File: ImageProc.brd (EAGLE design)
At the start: 44 x 23.2 mm, 96 parts, among them IC1 XC61GC3002HR-G, IC2 MIC5335-SPYMT, IC3 LTC6087, IC4 LTC6087, IC5 AT86RF233-ZU, IC7 DRV8833RTY, IC8 DRV8833RTY, IC9 MPU-6000, J1 CON-HRS-DM3AT, P1 BAT+, P10 MD2, P2 BAT-, P3 MA1, P4 MA2, P5 MB1, P6 MB2, P7 MC1, P8 MC2, P9 MD1, U1 CY8C5688LTI-LP086, U2 SIT8008AI-72-33E-24.000000G

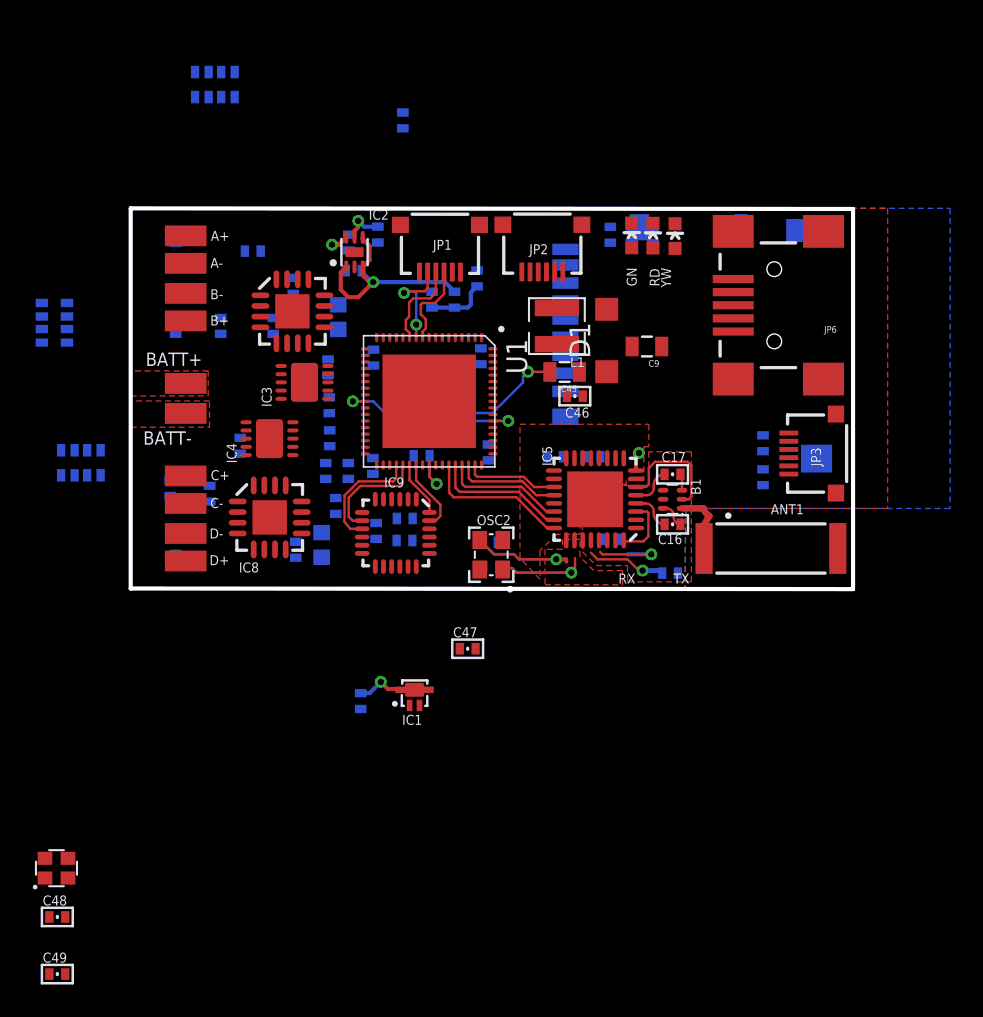
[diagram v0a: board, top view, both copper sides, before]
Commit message: Further routing. Moved 1K resistors to res array.
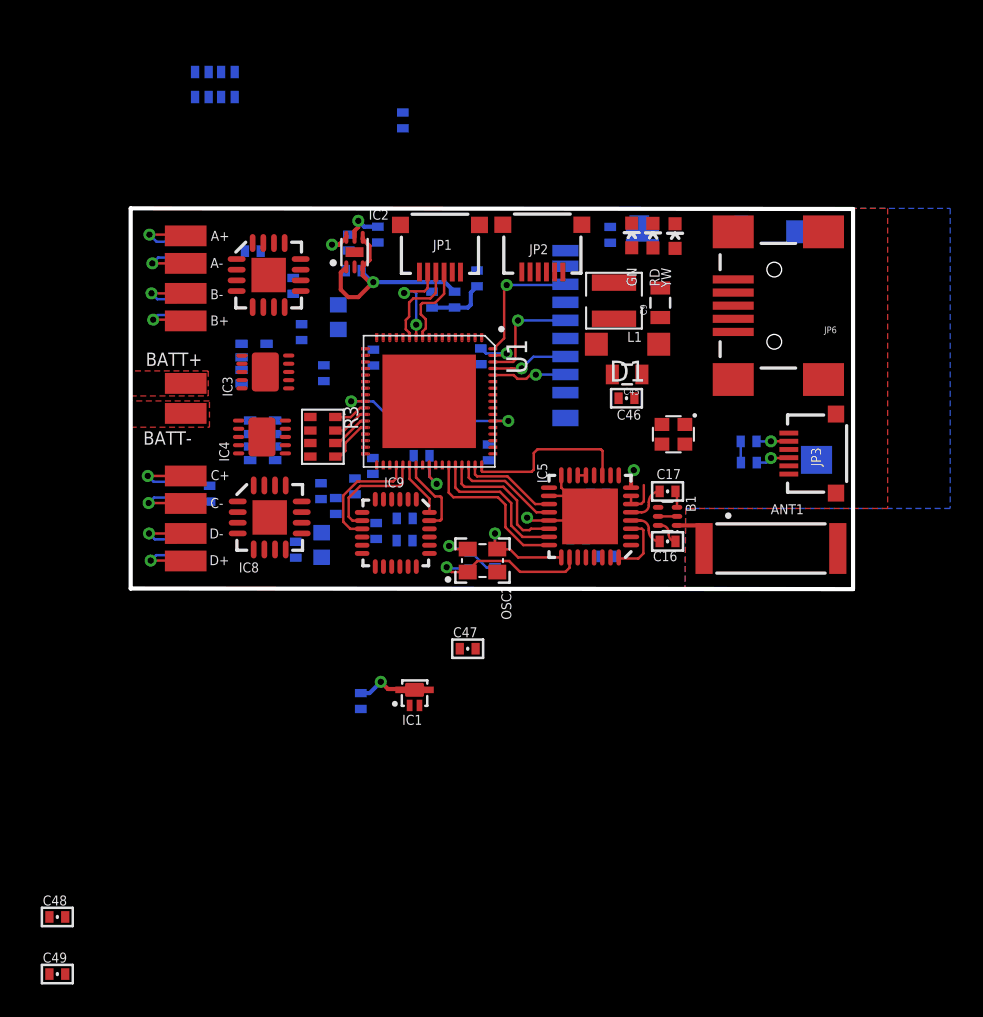
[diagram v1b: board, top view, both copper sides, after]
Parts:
- removed R29, R30, R31, R32: 1k, biomimetic:0402-RES
- added R3: 1K, OPL Eagle Library:R1206-8
- moved U2 46.0 mm to (33.1, 9.40), turned to 180 degrees
- moved R8 12.4 mm to (7.52, 13.7)
- moved R34 11.2 mm to (8.04, 9.03), turned to 90 degrees
- moved C21 5.97 mm to (27.3, 3.05), turned to 0 degrees
- moved C45 3.81 mm to (30.3, 13.0)
- moved L1 3.81 mm to (29.5, 17.5)
- moved C26 3.27 mm to (11.6, 5.93)
- moved C46 3.15 mm to (30.2, 11.6)
- moved C23 3.13 mm to (27.0, 5.11), turned to 270 degrees
- moved C9 2.79 mm to (32.3, 17.4), turned to 90 degrees
- moved IC7 2.64 mm to (8.41, 19.1)
- moved IC3 2.47 mm to (8.20, 13.2)
- moved C22 2.31 mm to (28.5, 5.74)
- moved C41 1.98 mm to (11.8, 13.1)
- moved C29 1.77 mm to (10.4, 15.6)
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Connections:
- removed net N$21: R4.1, U1.37
- net EMFILE_CS: now also U1.64; no longer U1.14
- net EMFILE_MISO: now also U1.68; no longer U1.15
- net EMFILE_MOSI: now also U1.65; no longer U1.16
- net EMFILE_SCK: now also U1.66; no longer U1.18
- net MOTOR_A_BEMF: now also R3.8, U1.27; no longer R29.2, U1.1
- net MOTOR_A_IN1: now also U1.2; no longer U1.28
- net MOTOR_A_IN2: now also U1.3; no longer U1.29
- net MOTOR_B_BEMF: now also R3.7, U1.28; no longer R30.2, U1.2
- net MOTOR_B_IN1: now also U1.4; no longer U1.30
- net MOTOR_C_BEMF: now also R3.6, U1.29; no longer R31.2, U1.3
- net MOTOR_D_BEMF: now also R3.5, U1.30; no longer R32.2, U1.4
- net N$34: now also R3.4; no longer R32.1
- net N$35: now also R3.3; no longer R31.1
- net N$36: now also R3.1; no longer R29.1
- net N$37: now also R3.2; no longer R30.1
- net SCL1: now also R4.1, U1.37
- net YW_LED: now also U1.1; no longer U1.27
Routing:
- net GND: track 11.1 -> 22.4 mm, vias 0 -> 2
- net RADIO_SLP_TR: track 0.00 -> 10.4 mm
- net EMFILE_MISO: track 0.00 -> 7.82 mm, vias 0 -> 1
- net VSSA: track 10.2 -> 3.19 mm, vias 2 -> 1
- net EMFILE_SCK: track 0.00 -> 6.74 mm, vias 0 -> 1
- net EMFILE_MOSI: track 0.00 -> 4.68 mm, vias 0 -> 1
- net N$8: track 10.9 -> 6.21 mm
- net N$3: track 4.64 -> 0.00 mm, vias 1 -> 0
- net EMFILE_CS: track 0.00 -> 4.58 mm, vias 0 -> 1
- net MOTOR_C_OUT1: track 0.00 -> 3.87 mm, vias 0 -> 1
- net MOTOR_C_OUT2: track 0.00 -> 3.77 mm, vias 0 -> 1
- net MOTOR_D_OUT2: track 0.00 -> 3.73 mm, vias 0 -> 1
- net MOTOR_A_OUT1: track 0.00 -> 3.72 mm, vias 0 -> 1
- net MOTOR_D_OUT1: track 0.00 -> 3.53 mm, vias 0 -> 1
- net 3.3V: track 7.39 -> 3.95 mm, vias 2 -> 1
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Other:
- board text removed: "RX"
- board text removed: "TX"

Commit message: More routing done. Many voltage domains merged to 3.3v and GND.
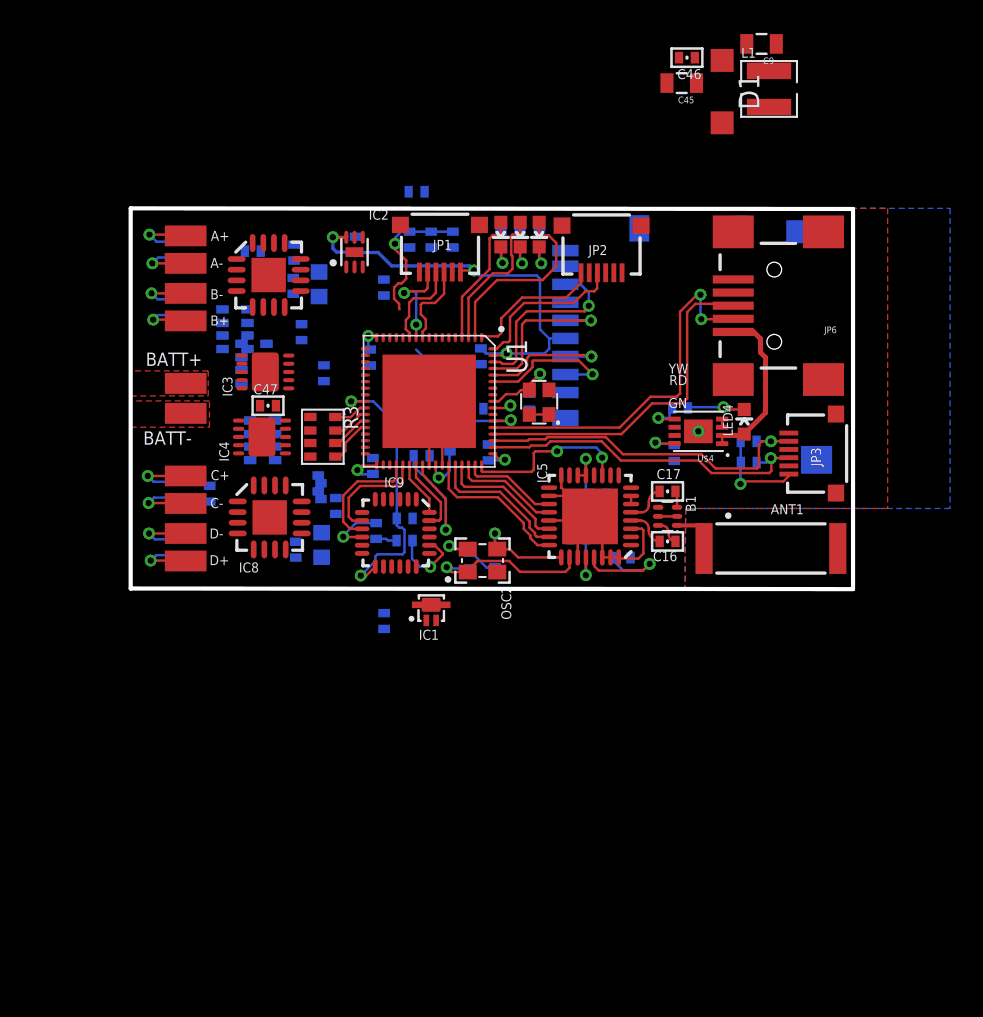
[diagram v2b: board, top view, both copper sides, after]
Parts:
- removed C49: 15pF, biomimetic:0402-CAP
- added LED4: YELLOW, biomimetic:LED-0603
- added R6, R7: 2K, biomimetic:0402-RES
- added U$4: MCP73831, pullin:DFN-8
- moved C48 42.6 mm to (24.3, 11.4), flipped to the bottom, turned to 270 degrees
- moved C46 21.1 mm to (33.9, 32.3)
- moved C47 19.2 mm to (8.37, 11.1)
- moved C45 18.1 mm to (33.6, 30.8)
- moved C9 16.9 mm to (38.4, 33.2), turned to 180 degrees
- moved D1 16.4 mm to (36.0, 30.3), turned to 270 degrees
- moved L1 16.0 mm to (38.9, 30.4), turned to 0 degrees
- moved R33 15.0 mm to (6.35, 15.8), turned to 270 degrees
- moved C32 10.4 mm to (9.96, 20.5)
- moved U2 8.46 mm to (24.9, 11.4), turned to 90 degrees
- moved LED3 8.28 mm to (24.9, 21.6), turned to 180 degrees
- moved LED2 8.09 mm to (23.7, 21.6), turned to 180 degrees
- moved LED1 7.98 mm to (22.6, 21.6), turned to 180 degrees
- moved R28 6.94 mm to (24.9, 21.4), turned to 90 degrees
- moved R27 6.81 mm to (23.7, 21.3), turned to 90 degrees
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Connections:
- net VBAT renamed V_BOOSTED_4.2V
- removed net N$33: JP6.VBUS
- removed net U2RX: JP2.6, U1.53
- removed net U2TX: JP2.4, U1.54
- removed net VDDA: C11.1, C13.1, U1.44
- removed net VDDD: C10.1, C12.1, C15.1, C2.1, C36.1, C45.1, C46.1, C5.1, C8.1, D1.C, U1.17, U1.24, U1.35, U1.52, U1.59, U1.67
- removed net VSSD: C10.2, C12.2, C15.2, C2.2, C36.2, C40.2, C5.2, C8.2, U1.CENTER_PAD
- new net 5V_USB: JP6.VBUS, LED4.A, U$4.1, U$4.2
- new net N$11: LED4.C, R7.1
- new net N$21: R7.2, U$4.5
- new net N$5: R6.1, U$4.8
- new net U1RX: JP2.6, U1.1
- new net U1TX: JP2.4, U1.68
- net 24MHZ: now also U2.3
- net 3.3V: now also C10.1, C11.1, C12.1, C13.1, C15.1, C2.1, C36.1, C45.1, C46.1, C5.1, C8.1, D1.C, U1.17, U1.24, U1.35, U1.44, U1.52, U1.59, U1.67; no longer C49.1
- net EMFILE_CS: now also U1.63; no longer U1.64
- net EMFILE_MISO: now also U1.66; no longer U1.68
- net EMFILE_MOSI: now also U1.64; no longer U1.65
- net EMFILE_SCK: now also U1.65; no longer U1.66
- net GND: now also C10.2, C11.2, C12.2, C14.2, C15.2, C2.2, C36.2, C40.2, C45.2, C46.2, C5.2, C8.2, R6.2, U$4.6, U$4.PAD, U1.43, U1.CENTER_PAD; no longer C49.2
- net GN_LED: now also U1.3; no longer U1.19
- net MOTOR_A_IN1: now also U1.13; no longer IC7.14, U1.2
- net MOTOR_A_IN2: now also U1.14; no longer IC7.13, U1.3
- net MOTOR_A_OUT1: no longer R33.1
- net MOTOR_A_OUT2: no longer R33.2
- net MOTOR_B_IN1: now also U1.15; no longer IC7.7, U1.4
- net MOTOR_B_IN2: no longer IC7.8
- net MOTOR_B_OUT1: no longer R33.3
- net MOTOR_B_OUT2: no longer R33.4
- net MOTOR_C_IN1: no longer IC8.14
- net MOTOR_C_IN2: no longer IC8.13
- net MOTOR_C_OUT1: no longer R34.1
- net MOTOR_C_OUT2: no longer R34.2
- net MOTOR_D_IN1: no longer IC8.7
- net MOTOR_D_IN2: now also U1.62; no longer IC8.8, U1.36
- net MOTOR_D_OUT1: no longer R34.3
- net MOTOR_D_OUT2: no longer R34.4
- net RD_LED: now also U1.2; no longer U1.23
- net SCL1: now also U1.53; no longer U1.37
- net SDA1: now also U1.54; no longer U1.21
- net VSSA: no longer C11.2, C14.2, C45.2, C46.2, U1.43
- net V_BATT: now also U$4.3, U$4.4
- net YW_LED: now also U1.4; no longer U1.1
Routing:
- net 3.3V: track 3.95 -> 63.1 mm, vias 1 -> 11
- net USB_D-: track 0.00 -> 22.4 mm, vias 0 -> 2
- net USB_D+: track 0.00 -> 21.0 mm
- net SDA1: track 1.97 -> 21.2 mm
- net SCL1: track 2.08 -> 20.8 mm
- net V_BATT: track 17.8 -> 0.50 mm, vias 2 -> 0
- net RD_LED: track 0.00 -> 11.3 mm
- net GND: track 22.4 -> 32.9 mm
- net 5V_USB: track 0.00 -> 10.2 mm
- net VCCA: track 0.00 -> 9.79 mm, vias 0 -> 1
- net U1TX: track 0.00 -> 9.63 mm
- net GN_LED: track 0.00 -> 9.13 mm
- net U1RX: track 0.00 -> 8.55 mm
- net YW_LED: track 0.00 -> 8.16 mm
- net N$3: track 0.00 -> 6.96 mm, vias 0 -> 1
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
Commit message: More routing. Starting to use rough paths just to set topology.
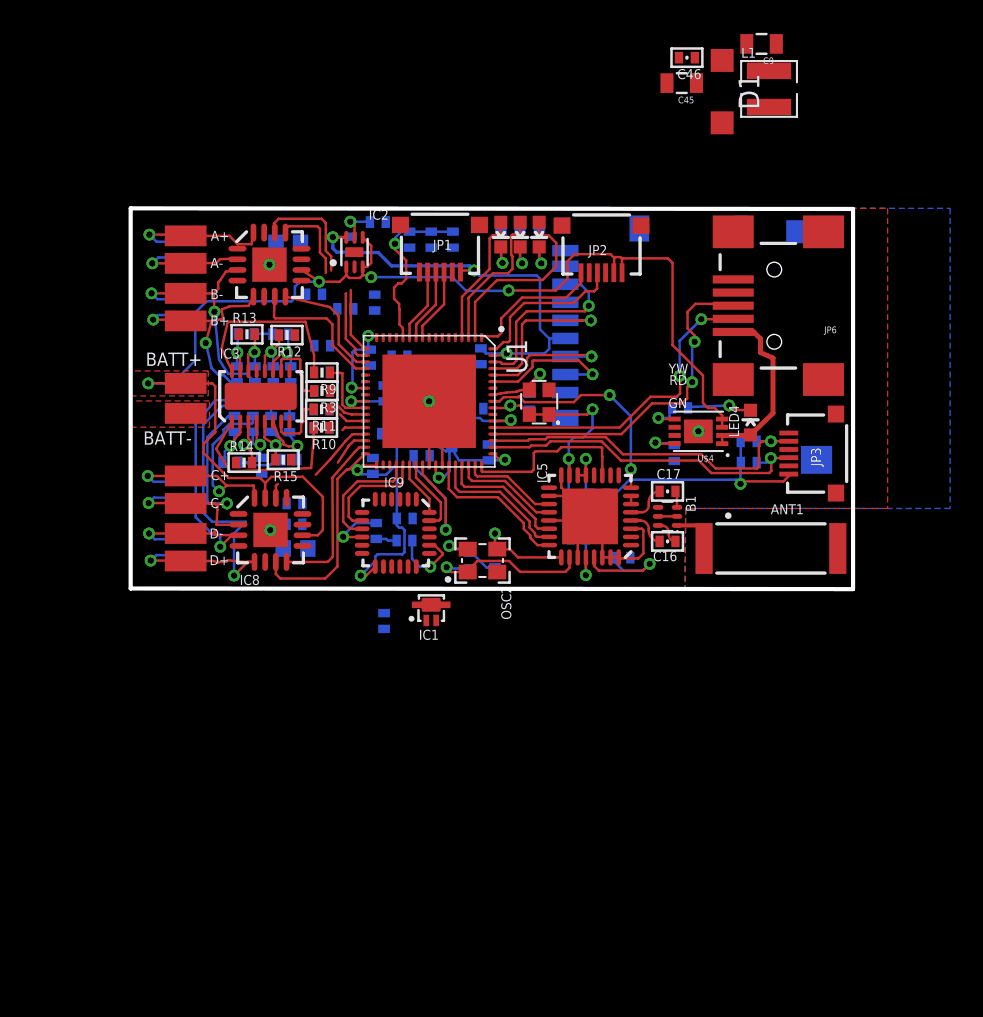
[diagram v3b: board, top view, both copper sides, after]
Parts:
- removed C29: 0.1uF, biomimetic:0402-CAP
- removed IC4: LTC6087, biomimetic:DFN-10
- removed R33, R34: 47k, OPL Eagle Library:R1206-8
- added R10, R11, R9: 1K, biomimetic:0402-RES
- added R12, R13, R14, R15, R16, R17, R18: 15K, biomimetic:0402-RES
- added R19, R20, R21, R22, R23, R24, R25, R29: 47k, biomimetic:0402-RES
- IC3: value LTC6087 -> LTC6088; device biomimetic:DFN-10 -> biomimetic:DFN-16
- R3: device OPL Eagle Library:R1206-8 -> biomimetic:0402-RES
- R8: value 15k -> 15K; device OPL Eagle Library:R1206-8 -> biomimetic:0402-RES
- moved C26 8.86 mm to (11.7, 14.8), turned to 0 degrees
- moved C42 8.51 mm to (11.7, 13.2), turned to 0 degrees
- moved C43 7.90 mm to (11.6, 9.79), turned to 0 degrees
- moved C32 4.64 mm to (13.1, 17.0), turned to 0 degrees
- moved C44 4.50 mm to (11.6, 10.9), turned to 0 degrees
- moved C40 4.49 mm to (15.5, 11.9), turned to 90 degrees
- moved C47 3.68 mm to (7.99, 7.48), flipped to the bottom, turned to 270 degrees
- moved C30 3.14 mm to (9.60, 21.1), turned to 0 degrees
- moved C7 3.00 mm to (15.1, 22.3)
- moved R3 2.79 mm to (11.7, 12.0), turned to 180 degrees
- moved C35 2.52 mm to (9.98, 5.18), turned to 0 degrees
- moved R8 2.40 mm to (9.12, 15.5), turned to 0 degrees
- moved C33 1.60 mm to (10.0, 2.44), turned to 0 degrees
- moved C34 1.55 mm to (9.98, 3.91), turned to 180 degrees
- moved IC3 1.51 mm to (7.92, 11.7), turned to 0 degrees
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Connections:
- new net RADIO_!RST: IC5.8, U1.60
- net !XRES: no longer IC5.8
- net 24MHZ: now also U1.61; no longer U1.60
- net 3.3V: now also IC3.4; no longer C29.1, IC3.10, IC4.10
- net BATT_LEVEL: now also U1.13; no longer U1.22
- net GND: now also IC3.13; no longer C29.2, IC3.4, IC4.4, IC4.PAD
- net MOTOR_A_BEMF: now also R3.1, U1.28; no longer R3.8, U1.27
- net MOTOR_A_IN1: now also IC7.14, U1.18; no longer U1.13
- net MOTOR_A_IN2: now also IC7.13, U1.19; no longer U1.14
- net MOTOR_A_OUT1: now also R29.2
- net MOTOR_A_OUT2: now also R25.2
- net MOTOR_B_BEMF: now also R9.1, U1.27; no longer R3.7, U1.28
- net MOTOR_B_IN1: now also IC7.7, U1.21; no longer U1.15
- net MOTOR_B_IN2: now also IC7.8, U1.20; no longer U1.31
- net MOTOR_B_OUT1: now also R23.2
- net MOTOR_B_OUT2: now also R24.2
- net MOTOR_C_BEMF: now also R10.1, U1.30; no longer R3.6, U1.29
- net MOTOR_C_IN1: now also IC8.14, U1.31; no longer U1.32
- net MOTOR_C_IN2: now also IC8.13, U1.32; no longer U1.33
- net MOTOR_C_OUT1: now also R22.2
- net MOTOR_C_OUT2: now also R21.2
- net MOTOR_D_BEMF: now also R11.1, U1.29; no longer R3.5, U1.30
- net MOTOR_D_IN1: now also IC8.7
- net MOTOR_D_IN2: now also IC8.8, U1.33; no longer U1.62
- net MOTOR_D_OUT1: now also R20.2
- net MOTOR_D_OUT2: now also R19.2
- net N$22: now also IC3.14, R13.2, R24.1; no longer IC3.7, R33.6, R8.2
- net N$23: now also IC3.15, R16.1, R23.1; no longer IC3.8, R33.5, R8.5
- net N$24: now also IC3.3, R14.2, R22.1; no longer IC4.3, R34.8
- net N$25: now also IC3.2, R17.1, R21.1; no longer IC4.2, R34.7
- net N$26: now also IC3.5, R15.2, R20.1; no longer IC4.7, R34.6
- net N$27: now also IC3.6, R18.1, R19.1; no longer IC4.8, R34.5
- net N$30: now also IC3.12, R12.2, R29.1; no longer IC3.3, R33.8, R8.1
- net N$31: now also IC3.11, R25.1, R8.1; no longer IC3.2, R33.7, R8.6
- net N$34: now also IC3.7, R11.2, R15.1; no longer IC4.9, R3.4
- net N$35: now also IC3.1, R10.2, R14.1; no longer IC4.1, R3.3
- net N$36: now also IC3.10, R12.1, R3.2; no longer IC3.1, R3.1, R8.8
- net N$37: now also IC3.16, R13.1, R9.2; no longer IC3.9, R3.2, R8.7
- net SWD_SCLK: now also JP1.5; no longer JP1.4
- net SWD_SDAT: now also JP1.4; no longer JP1.5
- net V_REF: now also R16.2, R17.2, R18.2, R8.2, U1.23; no longer R8.3, R8.4
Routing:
- net V_BATT: track 0.50 -> 78.6 mm, vias 0 -> 4
- net 3.3V: track 63.1 -> 99.1 mm, vias 11 -> 15
- net MOTOR_D_OUT1: track 3.53 -> 26.3 mm, vias 1 -> 2
- net MOTOR_D_OUT2: track 3.73 -> 24.4 mm, vias 1 -> 2
- net RADIO_!RST: track 0.00 -> 13.7 mm, vias 0 -> 2
- net MOTOR_D_IN1: track 0.00 -> 12.5 mm
- net MOTOR_C_OUT2: track 3.77 -> 16.3 mm, vias 1 -> 2
- net MOTOR_C_OUT1: track 3.87 -> 16.2 mm, vias 1 -> 2
- net N$37: track 0.00 -> 11.1 mm
- net N$35: track 0.00 -> 10.9 mm
- net MOTOR_B_OUT2: track 3.42 -> 14.4 mm, vias 1 -> 2
- net MOTOR_A_IN1: track 0.00 -> 10.9 mm
- net MOTOR_D_IN2: track 0.00 -> 10.6 mm
- net MOTOR_B_OUT1: track 3.22 -> 13.3 mm, vias 1 -> 2
- net MOTOR_A_IN2: track 0.00 -> 9.84 mm
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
